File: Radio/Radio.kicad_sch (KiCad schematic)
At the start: 20 parts, among them U1 LM386, U2 RDA5807M_Module, U3 LM386

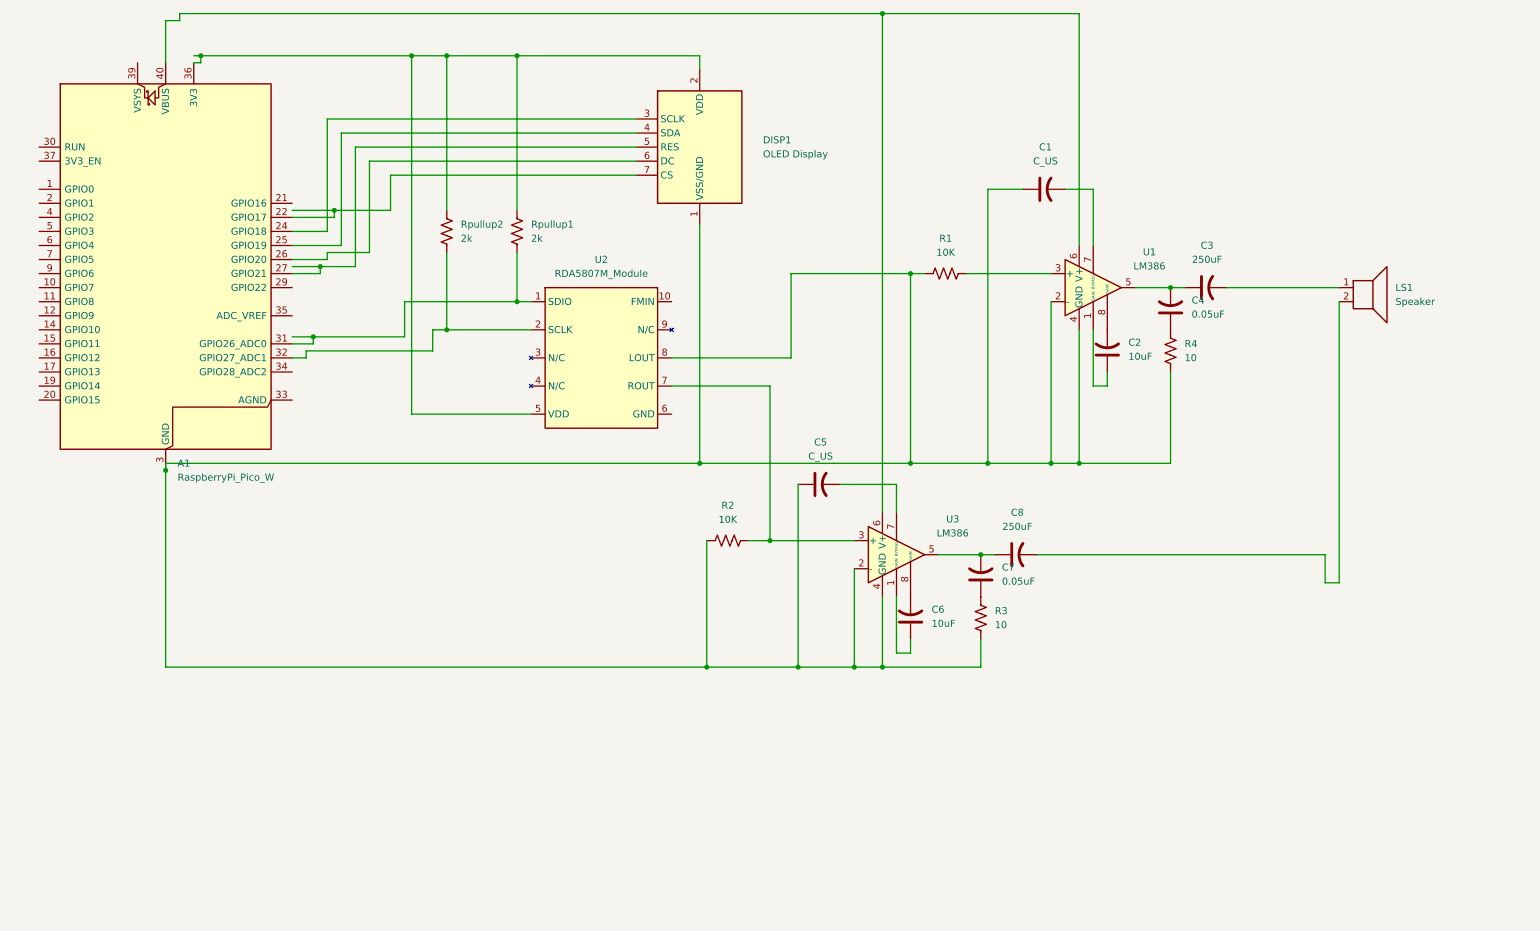
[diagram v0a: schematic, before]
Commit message: added 2 rotary encoders and 4 buttons
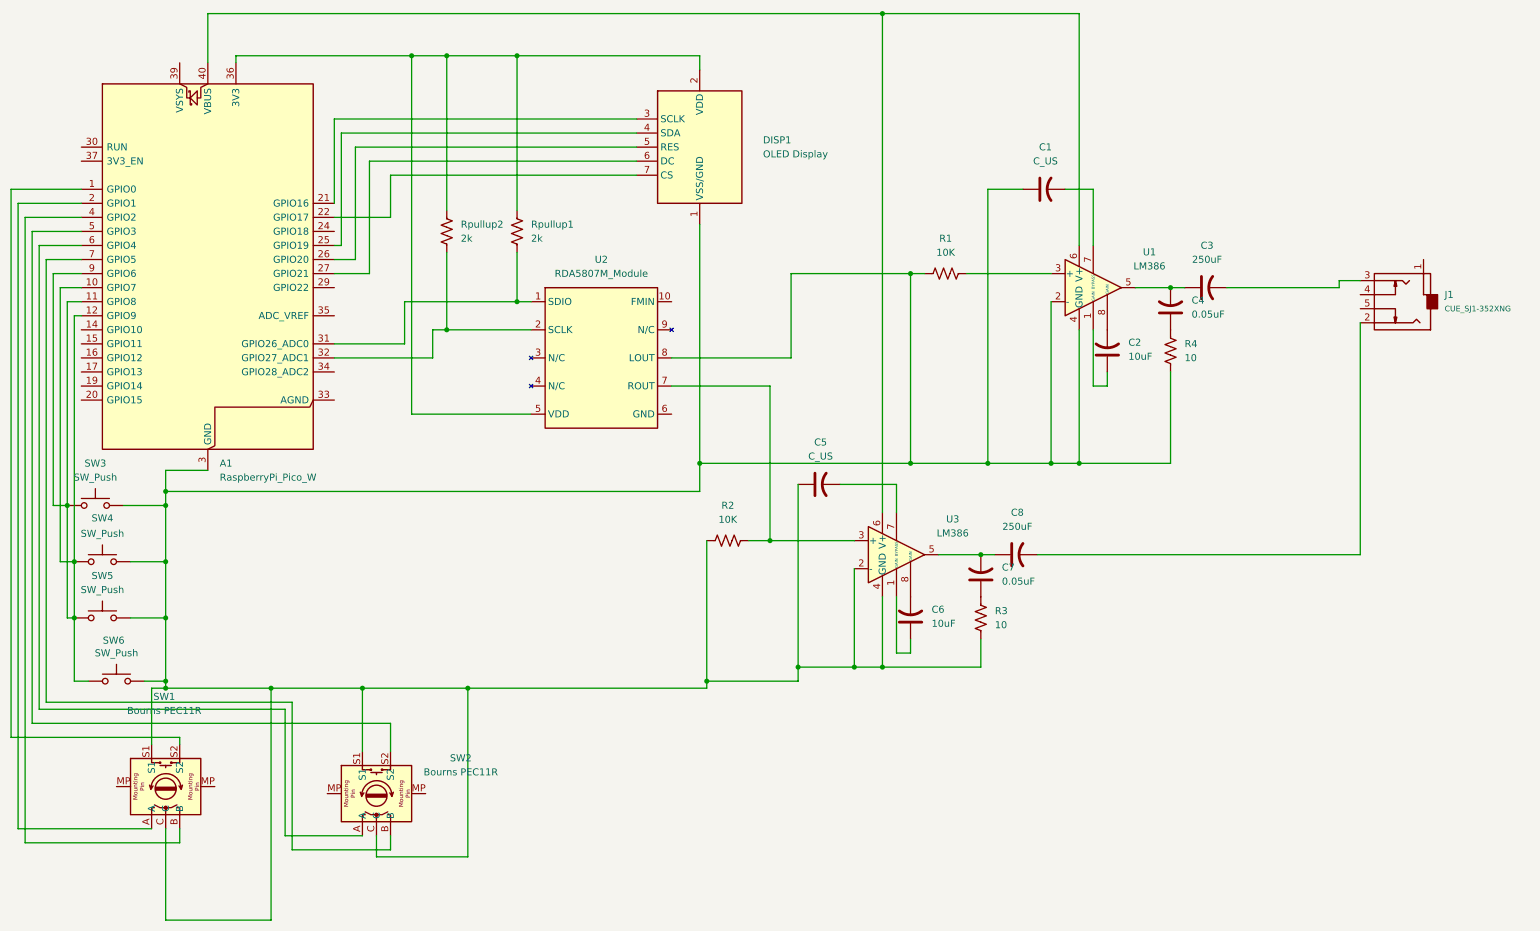
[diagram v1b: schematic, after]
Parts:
- removed LS1: Speaker, symbol Device:Speaker
- added J1: CUE_SJ1-352XNG, symbol ECE:CUE_SJ1-352XNG
- added SW1, SW2: Bourns PEC11R, Rotary_Encoder:RotaryEncoder_Alps_EC12E-Switch_Vertical_H20mm, symbol ECE:Bourns PEC11R
- added SW3, SW4, SW5, SW6: SW_Push, symbol Switch:SW_Push
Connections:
- net at A1.13 (GND), A1.18 (GND), A1.23 (GND)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: now also SW1.C, SW1.S1, SW2.C, SW2.S1, SW3.2, SW4.2, SW5.2, SW6.2
- net at C3.2: now also J1.3 (Tip)
- net at C8.2: now also J1.2 (Tip)
- net at DISP1.3 (SCLK): now also A1.21 (GPIO16); no longer A1.24 (GPIO18)
- net at DISP1.5 (RES): now also A1.26 (GPIO20); no longer A1.27 (GPIO21)
- net at DISP1.6 (DC): now also A1.27 (GPIO21); no longer A1.26 (GPIO20)
- net at A1.1 (GPIO0): now also SW1.S2
- net at A1.10 (GPIO7): now also A1.11 (GPIO8), A1.12 (GPIO9), A1.9 (GPIO6), SW3.1, SW4.1, SW5.1, SW6.1
- net at A1.2 (GPIO1): now also SW1.A
- net at A1.4 (GPIO2): now also SW1.B
- net at A1.5 (GPIO3): now also SW2.S2
- net at A1.6 (GPIO4): now also SW2.A
- net at A1.7 (GPIO5): now also SW2.B
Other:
- moved on the sheet: A1

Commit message: Fixed some of schematic and added footprints. Added schematic to the PCB editor and now I got to redesign the schematic so all connections work
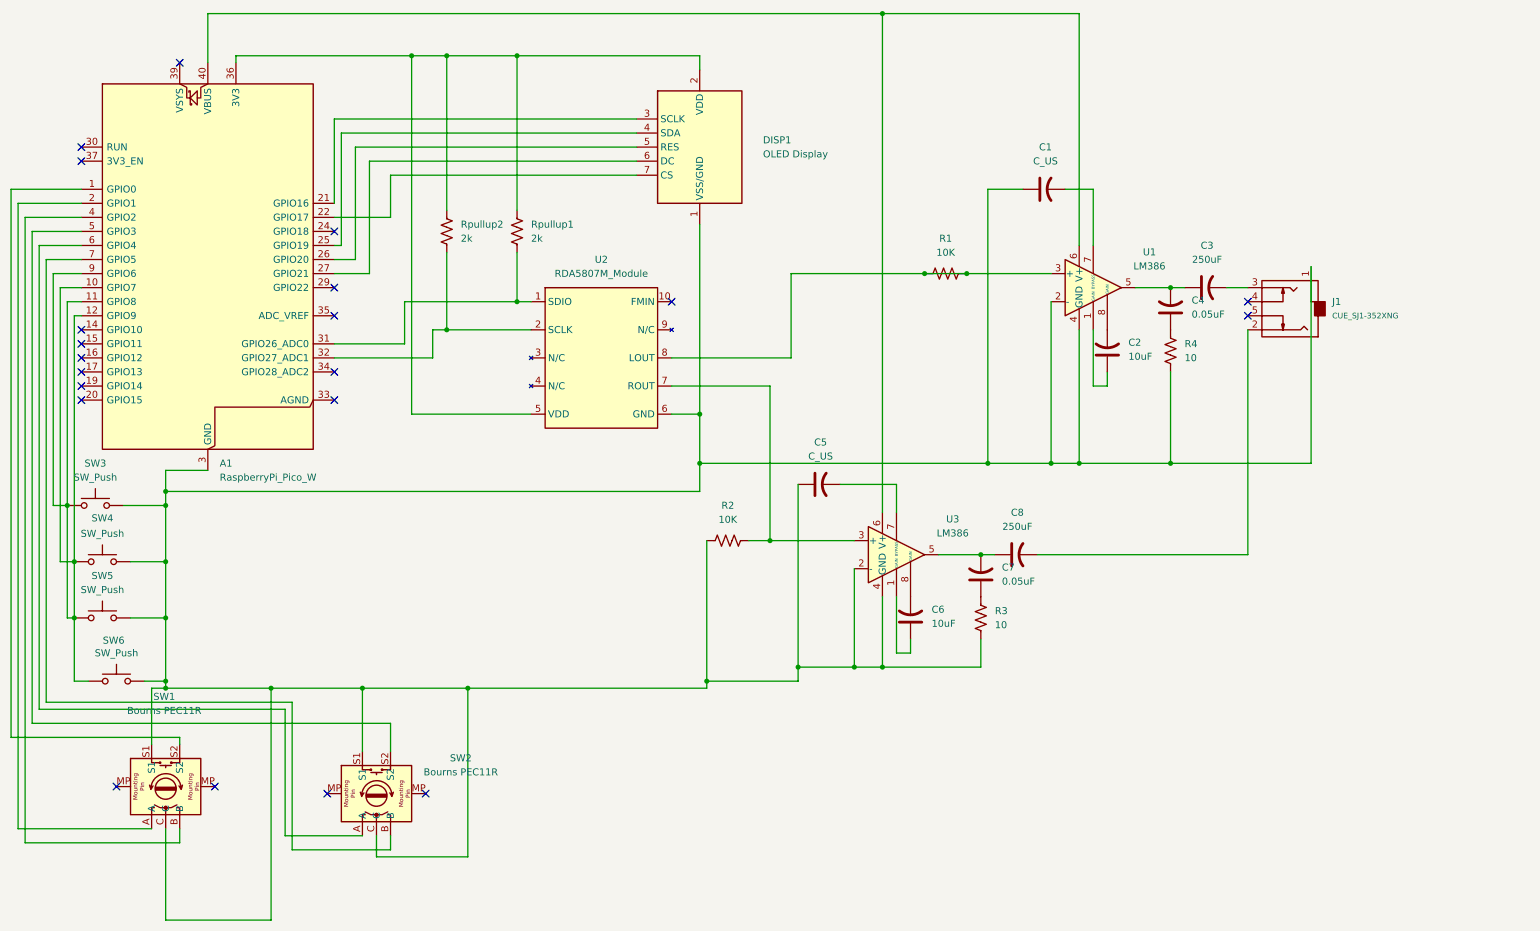
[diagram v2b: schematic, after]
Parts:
- C1, C2, C3, C4, C5, C6, C7, C8: footprint (none) -> Capacitor_THT:C_Rect_L4.0mm_W2.5mm_P2.50mm
- DISP1: footprint (none) -> ECE:OLED_Display_1.3
- J1: footprint (none) -> ECE:CUE_SJ1-352XNG
- R1, R2, R3, R4, Rpullup1, Rpullup2: footprint (none) -> Resistor_THT:R_Axial_DIN0204_L3.6mm_D1.6mm_P5.08mm_Horizontal
- SW3, SW4, SW5, SW6: footprint (none) -> Button_Switch_THT:SW_PUSH_6mm
- U1, U3: footprint (none) -> Package_DIP:DIP-8_W7.62mm_Socket
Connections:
- net at A1.13 (GND), A1.18 (GND), A1.23 (GND)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: now also J1.1 (Sleeve), U2.6 (GND); no longer R1.1, U2.8 (LOUT)
- net at R1.2, U1.3 (+): now also R1.1, U2.8 (LOUT)
- no-connect marks 0 -> 21
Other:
- moved on the sheet: J1

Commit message: Finished making first version of the pcb design. Added fornt and back copper and filled the back with copper. Also removed one of the two amplifiers.
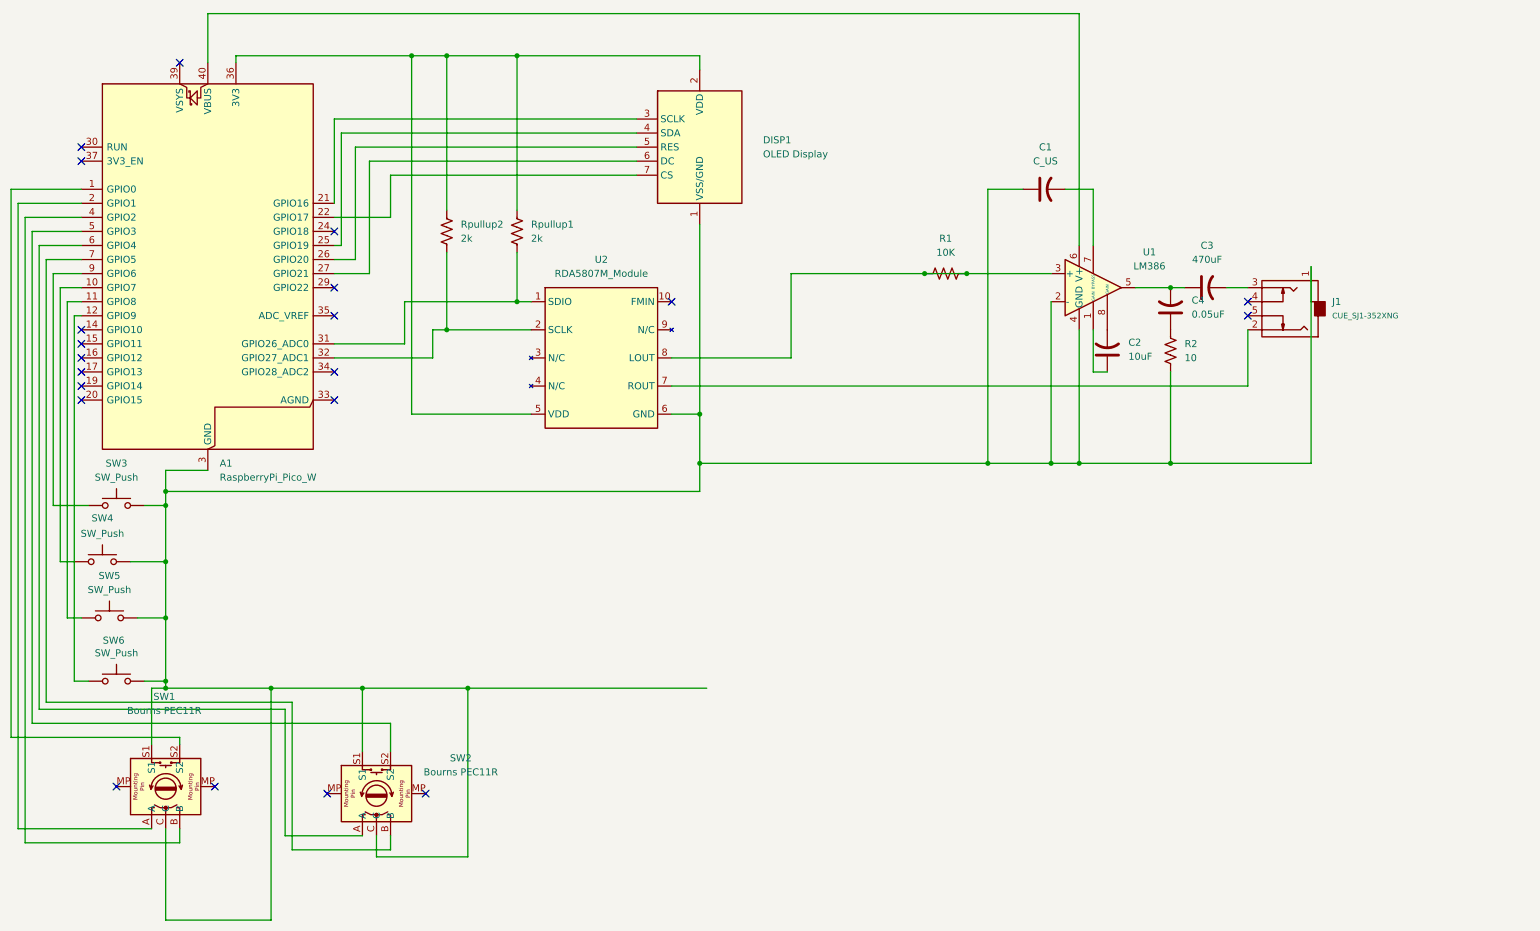
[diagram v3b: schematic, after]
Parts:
- removed C5: C_US, Capacitor_THT:C_Rect_L4.0mm_W2.5mm_P2.50mm, symbol Device:C_US
- removed C6: 10uF, Capacitor_THT:C_Rect_L4.0mm_W2.5mm_P2.50mm, symbol Device:C_US
- removed C7: 0.05uF, Capacitor_THT:C_Rect_L4.0mm_W2.5mm_P2.50mm, symbol Device:C_US
- removed C8: 250uF, Capacitor_THT:C_Rect_L4.0mm_W2.5mm_P2.50mm, symbol Device:C_US
- removed R2: 10K, Resistor_THT:R_Axial_DIN0204_L3.6mm_D1.6mm_P5.08mm_Horizontal, symbol Device:R_US
- removed R3: 10, Resistor_THT:R_Axial_DIN0204_L3.6mm_D1.6mm_P5.08mm_Horizontal, symbol Device:R_US
- removed U3: LM386, Package_DIP:DIP-8_W7.62mm_Socket, symbol Amplifier_Audio:LM386
- C3: value 250uF -> 470uF
- renumbered R4 to R2
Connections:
- net at U2.7 (ROUT): now also J1.2 (Tip)
- new net: A1.9 (GPIO6), SW3.1
- new net: A1.12 (GPIO9), SW6.1
- new net: A1.11 (GPIO8), SW5.1
- new net: A1.10 (GPIO7), SW4.1
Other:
- moved on the sheet: SW3, SW5

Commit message: Add files via upload
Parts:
- removed J1: CUE_SJ1-352XNG, ECE:CUE_SJ1-352XNG, symbol ECE:CUE_SJ1-352XNG
- removed SW5, SW6: SW_Push, Button_Switch_THT:SW_PUSH_6mm, symbol Switch:SW_Push
- added LS1: Speaker, Buzzer_Beeper:Speaker_CUI_CMR-1206S-67, symbol Device:Speaker
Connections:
- net at C3.2: now also LS1.1
- net at U2.7 (ROUT): now also LS1.2
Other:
- moved on the sheet: A1, SW3, SW4

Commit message: Updated Schematic
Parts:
- added C5: 10uF, Capacitor_THT:C_Rect_L4.0mm_W2.5mm_P2.50mm, symbol Device:C_US
- added R3, R4, R5, R6: 10K, Resistor_THT:R_Axial_DIN0204_L3.6mm_D1.6mm_P5.08mm_Horizontal, symbol Device:R_US
- C1: value C_US -> 10uF
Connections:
- net at A1.13 (GND), A1.18 (GND), A1.23 (GND)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: now also LS1.2, R1.1; no longer SW1.S1, SW2.S1, SW3.2, SW4.2
- net at SW1.A: now also R3.1; no longer A1.2 (GPIO1)
- net at SW1.B: now also R4.1; no longer A1.4 (GPIO2)
- net at R1.2, U2.8 (LOUT): now also U2.7 (ROUT), C5.1; no longer R1.1, U1.3 (+)
- net at SW2.A: now also R5.1; no longer A1.6 (GPIO4)
- net at SW2.B: now also R6.1; no longer A1.7 (GPIO5)
- net at A1.36 (3V3), DISP1.2 (VDD), Rpullup1.1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: now also SW1.S1, SW2.S1, SW3.2, SW4.2
- new net: A1.7 (GPIO5), R6.2
- new net: C5.2, U1.3 (+)
- new net: A1.2 (GPIO1), R3.2
- new net: A1.6 (GPIO4), R5.2
- new net: A1.4 (GPIO2), R4.2
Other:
- moved on the sheet: R1
